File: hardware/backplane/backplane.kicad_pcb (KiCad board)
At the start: 2 copper layers, 199 x 123 mm, 83 parts, among them J1 C96ABC, J10 Conn_Coaxial_Power, J2 C96ABC, J3 C96ABC, J4 C96ABC, J5 C96ABC, J6 C96ABC, J7 C96ABC, J8 C96ABC, J9 C96ABC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

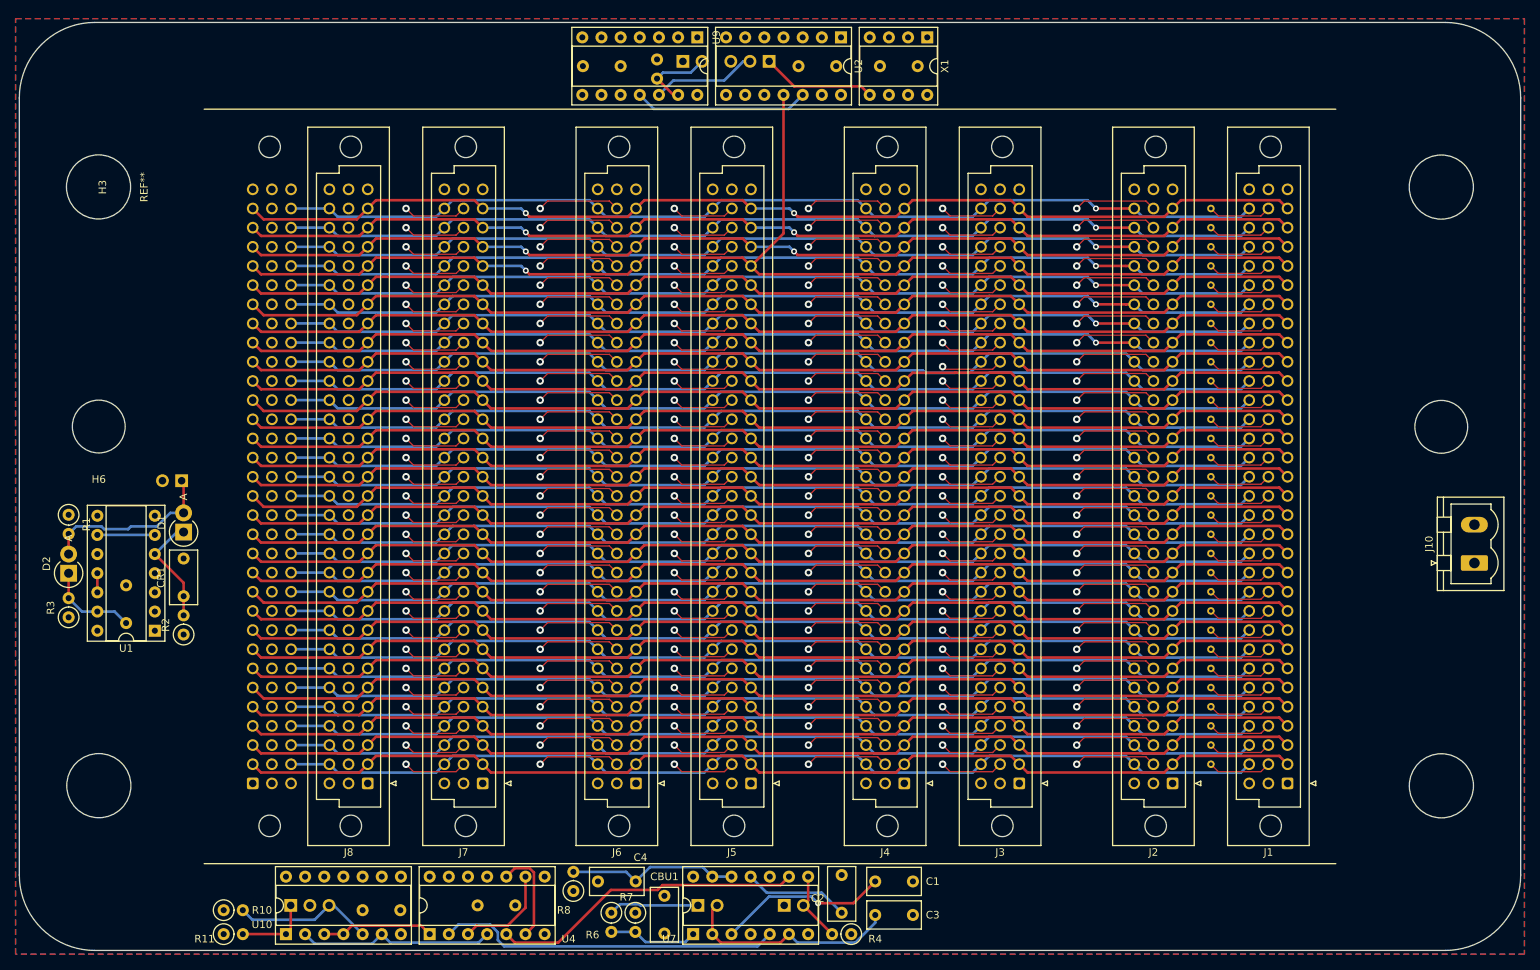
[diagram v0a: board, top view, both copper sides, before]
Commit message: backplane: use mostly SMD parts
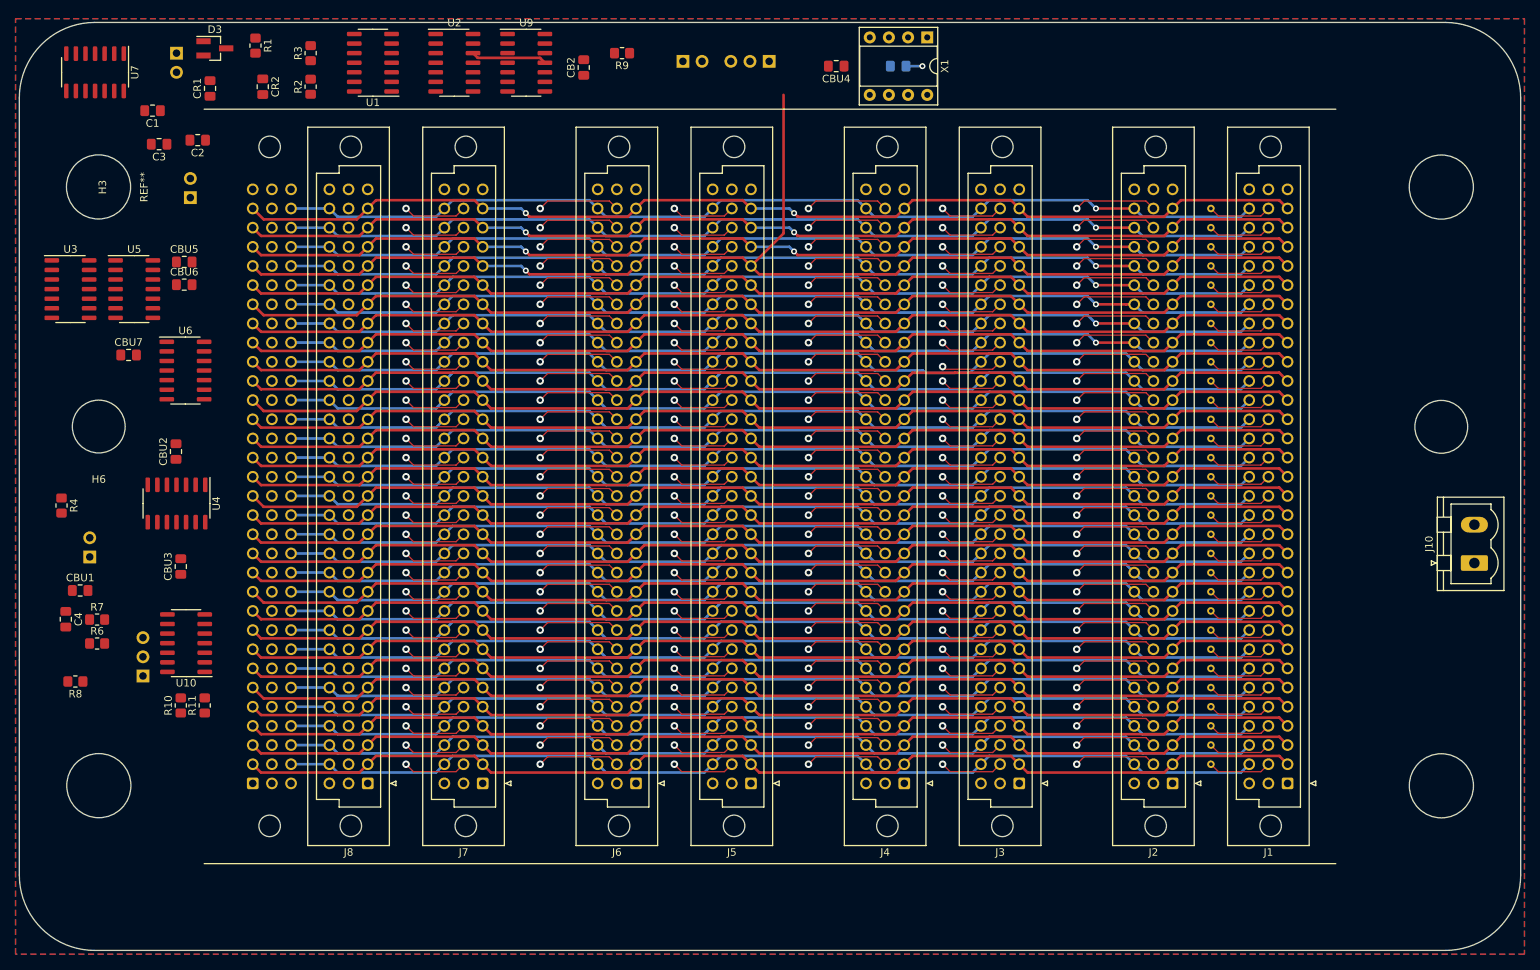
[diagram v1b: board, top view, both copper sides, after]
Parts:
- removed D1, D2: DIODE, Diode_THT:D_DO-15_P2.54mm_Vertical_AnodeUp
- added CBU5: 0.1μF, Capacitor_SMD:C_0805_2012Metric_Pad1.18x1.45mm_HandSolder, F.Cu at (66.4, 60.8)
- added CBU6: 0.1μF, Capacitor_SMD:C_0805_2012Metric_Pad1.18x1.45mm_HandSolder, F.Cu at (66.4, 63.8)
- added CBU7: 0.1μF, Capacitor_SMD:C_0805_2012Metric_Pad1.18x1.45mm_HandSolder, F.Cu at (59.1, 73.1)
- added D3: D_Schottky_x2_KCom_AAK, Package_TO_SOT_SMD:SOT-23_Handsoldering, F.Cu at (70.5, 32.5)
- added U3: 74AHC74, Package_SO:SOIC-14_3.9x8.7mm_P1.27mm, F.Cu at (51.4, 64.4)
- added U5: 74AHC74, Package_SO:SOIC-14_3.9x8.7mm_P1.27mm, F.Cu at (59.8, 64.4)
- added U6: 74AHC02, Package_SO:SOIC-14_3.9x8.7mm_P1.27mm, F.Cu at (66.6, 75.2)
- C1, C2, C3, C4, CBU1, CBX1, CR1: footprint Capacitor_THT:C_Rect_L7.0mm_W3.5mm_P5.00mm -> Capacitor_SMD:C_0805_2012Metric_Pad1.18x1.45mm_HandSolder
- CB2, CBU2, CBU3, CBU4, CR2: footprint Capacitor_THT:C_Rect_L7.0mm_W3.5mm_P5.00mm -> Capacitor_SMD:C_0805_2012Metric_Pad1.18x1.45mm_HandSolder; moved to F.Cu
- R1, R10, R11, R2, R3, R4, R6, R7, R8: footprint Resistor_THT:R_Axial_DIN0207_L6.3mm_D2.5mm_P2.54mm_Vertical -> Resistor_SMD:R_0805_2012Metric_Pad1.20x1.40mm_HandSolder
- R9: footprint Resistor_THT:R_Axial_DIN0207_L6.3mm_D2.5mm_P2.54mm_Vertical -> Resistor_SMD:R_0805_2012Metric_Pad1.20x1.40mm_HandSolder; moved to F.Cu
- U1, U2, U4, U7, U9: footprint Package_DIP:DIP-14_W7.62mm_Socket -> Package_SO:SOIC-14_3.9x8.7mm_P1.27mm
- U10: value U13 -> 74HC00; footprint Package_DIP:DIP-14_W7.62mm_Socket -> Package_SO:SOIC-14_3.9x8.7mm_P1.27mm
- moved C1 140.0 mm to (62.2, 40.7), turned to 180 degrees
- moved C3 139.5 mm to (63.1, 45.2), turned to 180 degrees
- moved U7 139.0 mm to (54.6, 35.6), turned to 270 degrees
- moved C2 133.3 mm to (68.2, 44.6), turned to 180 degrees
- moved SW1 122.5 mm to (67.2, 52.2), turned to 0 degrees
- moved R4 119.1 mm to (50.2, 93.0), turned to 270 degrees
- moved R5 92.9 mm to (53.9, 99.9), turned to 0 degrees
- moved CBU1 87.4 mm to (52.6, 104.3), turned to 0 degrees
- moved C4 83.1 mm to (50.7, 108.1), turned to 270 degrees
- moved R3 81.4 mm to (83.2, 33.1)
- moved R7 81.2 mm to (54.9, 108.2), turned to 0 degrees
- moved U1 80.6 mm to (91.5, 34.4)
- moved R6 76.9 mm to (54.9, 111.3), turned to 0 degrees
- moved R2 74.5 mm to (83.2, 37.5)
- moved CR2 73.4 mm to (76.8, 37.5), turned to 270 degrees
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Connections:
- net Net-(U4-Pad11) renamed PHI_2
- U1 pad 1: GND -> A31
- U1 pad 3: GND -> A28
- U10 pad 10: GND -> Net-(U10-Pad10)
- U10 pad 12: GND -> Net-(U10-Pad12)
- U10 pad 13: GND -> A28
- U10 pad 9: GND -> A31
- U2 pad 4: GND -> Net-(U2-Pad4)
- U2 pad 5: GND -> A27
- U4 pad 12: GND -> Net-(U10-Pad8)
- U4 pad 13: GND -> Net-(U10-Pad11)
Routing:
- net 555_AST: track 45.5 -> 0.00 mm
- net 555_MONO: track 41.6 -> 0.00 mm
- net Net-(C3-Pad1): track 29.2 -> 0.00 mm
- net SEL_MONO: track 26.1 -> 0.00 mm
- net ~RST_HDR~: track 23.7 -> 0.00 mm
- net Net-(C4-Pad1): track 22.8 -> 0.00 mm
- net Net-(C1-Pad1): track 22.7 -> 0.00 mm, vias 1 -> 0
- net Net-(R10-Pad2): track 18.8 -> 0.00 mm
- net XO: track 15.2 -> 0.00 mm
- net SEL_AST: track 14.9 -> 0.00 mm
- net Net-(CR1-Pad1): track 14.7 -> 0.00 mm
- net Net-(C2-Pad1): track 14.0 -> 0.00 mm
- net Net-(SW2-Pad2): track 13.9 -> 0.00 mm
- net Net-(U4-Pad3): track 13.2 -> 0.00 mm
- net Net-(U2-Pad12): track 23.1 -> 10.1 mm
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
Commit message: backplane: place traces
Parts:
- removed the CBU4 at (152.9, 34.8)
- removed R9: 4.7k, Resistor_SMD:R_0805_2012Metric_Pad1.20x1.40mm_HandSolder
- removed U9: 74AHCT125, Package_SO:SOIC-14_3.9x8.7mm_P1.27mm
- added CBU7: 0.1μF, Capacitor_SMD:C_0805_2012Metric_Pad1.18x1.45mm_HandSolder, B.Cu at (65.6, 108.6)
- added CBU8: 0.1μF, Capacitor_SMD:C_0805_2012Metric_Pad1.18x1.45mm_HandSolder, B.Cu at (67.1, 83.0)
- added U8: 74HC00, Package_SO:SOIC-14_3.9x8.7mm_P1.27mm, F.Cu at (66.8, 84.2)
- C1, C2, C3, C4, CBU1, CR1, CR2, X1: moved to B.Cu
- CBU10: renamed from CBU3; moved to B.Cu
- CBU2: renamed from CB2; moved to B.Cu
- CBU3: renamed from CBU5; moved to B.Cu
- CBU4: renamed from CBU2; moved to B.Cu
- CBU5: renamed from CBU6; moved to B.Cu
- CBU6: renamed from CBU7; moved to B.Cu
- CBX1: moved to F.Cu
- R1: value 4.7k -> 1k
- moved X1 134.1 mm to (70.0, 125.8), turned to 90 degrees
- moved CBX1 128.4 mm to (66.6, 121.7)
- moved SW2 121.6 mm to (57.3, 119.5)
- moved JP1 113.6 mm to (53.5, 115.7), turned to 0 degrees
- moved CBU2 78.2 mm to (49.1, 69.1), turned to 270 degrees
- moved U7 74.9 mm to (65.6, 109.8), turned to 0 degrees
- moved C1 71.2 mm to (63.0, 111.9), turned to 270 degrees
- moved C2 68.0 mm to (71.0, 112.6), turned to 270 degrees
- moved U2 64.0 mm to (49.4, 70.5)
- moved C3 62.1 mm to (63.0, 107.2), turned to 90 degrees
- moved SW1 61.7 mm to (57.3, 113.2), turned to 180 degrees
- moved CBU1 45.5 mm to (68.6, 61.7), turned to 270 degrees
- moved U1 36.4 mm to (68.2, 62.4), turned to 0 degrees
- moved R11 31.0 mm to (47.0, 97.8)
- moved SW3 30.2 mm to (48.2, 88.3), turned to 180 degrees
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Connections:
- net PHI_2 renamed Net-(U4-Pad11)
- D3 pad 1: Net-(CR1-Pad1) -> Net-(CR2-Pad1)
- D3 pad 2: Net-(CR2-Pad1) -> Net-(CR1-Pad1)
- JP1 pad 1: GND -> Net-(JP1-Pad1)
- JP1 pad 2: ~CLK_ENABLE~ -> Net-(JP1-Pad2)
- SW2 pad 2: Net-(SW2-Pad2) -> Net-(JP1-Pad1)
- U10 pad 10: Net-(U10-Pad10) -> SEL_AST
- U10 pad 12: Net-(U10-Pad12) -> SEL_MONO
- U10 pad 13: A28 -> 555_MONO
- U10 pad 9: A31 -> 555_AST
- U2 pad 11: A28 -> Net-(U2-Pad11)
- U2 pad 12: Net-(U2-Pad12) -> GND
- U2 pad 13: ~CLK_RST~ -> GND
- U3 pad 9: Net-(U10-Pad10) -> Net-(U3-Pad9)
- U4 pad 1: SEL_AST -> Net-(JP1-Pad2)
- U4 pad 10: Net-(U4-Pad10) -> Net-(U10-Pad11)
- U4 pad 12: Net-(U10-Pad8) -> GND
- U4 pad 13: Net-(U10-Pad11) -> GND
- U4 pad 2: 555_AST -> ~CLK_RST~
- U4 pad 4: SEL_MONO -> Net-(U4-Pad3)
- U4 pad 5: 555_MONO -> Net-(U4-Pad3)
- U4 pad 6: Net-(U4-Pad10) -> A28
- U4 pad 9: Net-(U4-Pad3) -> Net-(U10-Pad8)
- U5 pad 9: Net-(U10-Pad12) -> Net-(U5-Pad9)
- U6 pad 3: Net-(U10-Pad12) -> Net-(U5-Pad9)
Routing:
- net ~CLK_RST~: track 0.00 -> 75.5 mm, vias 0 -> 4
- net C13: track 133.4 -> 208.1 mm
- net A28: track 168.9 -> 221.6 mm, vias 1 -> 4
- net GND: track 0.00 -> 42.8 mm, vias 0 -> 16
- net A31: track 144.7 -> 185.0 mm, vias 2 -> 4
- net A27: track 144.5 -> 179.7 mm
- net 555_CLK: track 0.00 -> 33.8 mm, vias 0 -> 1
- net Net-(JP1-Pad2): track 0.00 -> 30.7 mm, vias 0 -> 1
- net VCC: track 2.18 -> 30.1 mm, vias 1 -> 13
- net Net-(U5-Pad9): track 0.00 -> 25.1 mm, vias 0 -> 2
- net 555_MONO: track 0.00 -> 22.5 mm, vias 0 -> 2
- net Net-(U1-Pad2): track 0.00 -> 22.1 mm, vias 0 -> 2
- net Net-(U2-Pad6): track 0.00 -> 20.8 mm, vias 0 -> 2
- net Net-(U2-Pad4): track 0.00 -> 19.7 mm
- net Net-(C3-Pad1): track 0.00 -> 19.4 mm, vias 0 -> 2
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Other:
- board text removed: "Clock adjust"
- board text removed: "Step"
- board text removed: "astable/mono toggle"

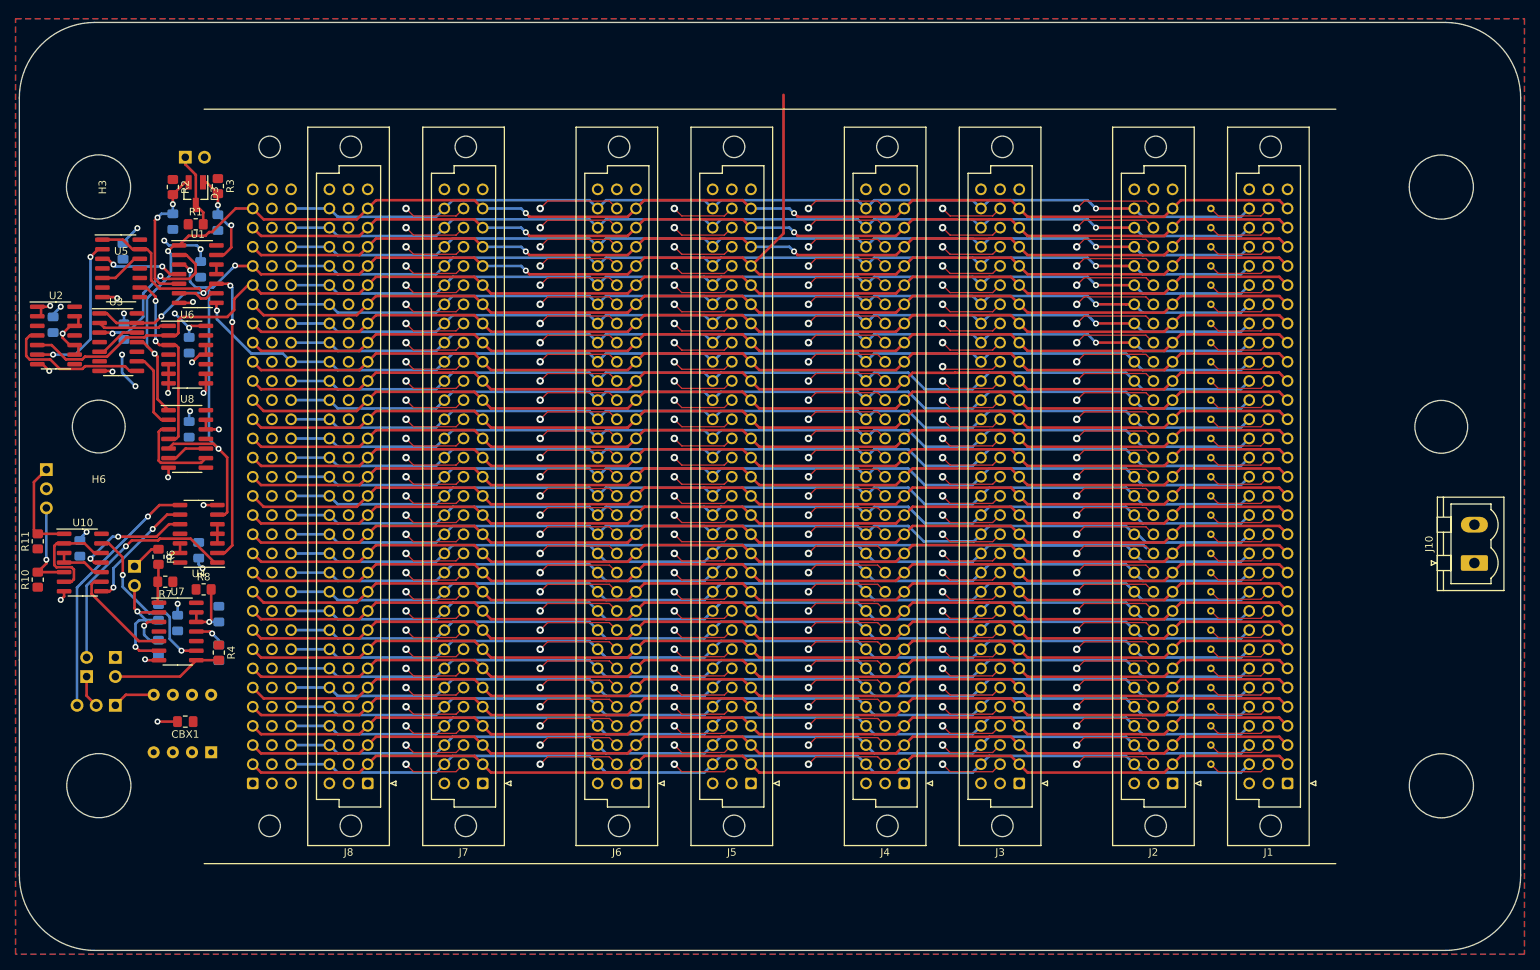
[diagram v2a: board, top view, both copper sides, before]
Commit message: backplane: tweak mounting holes
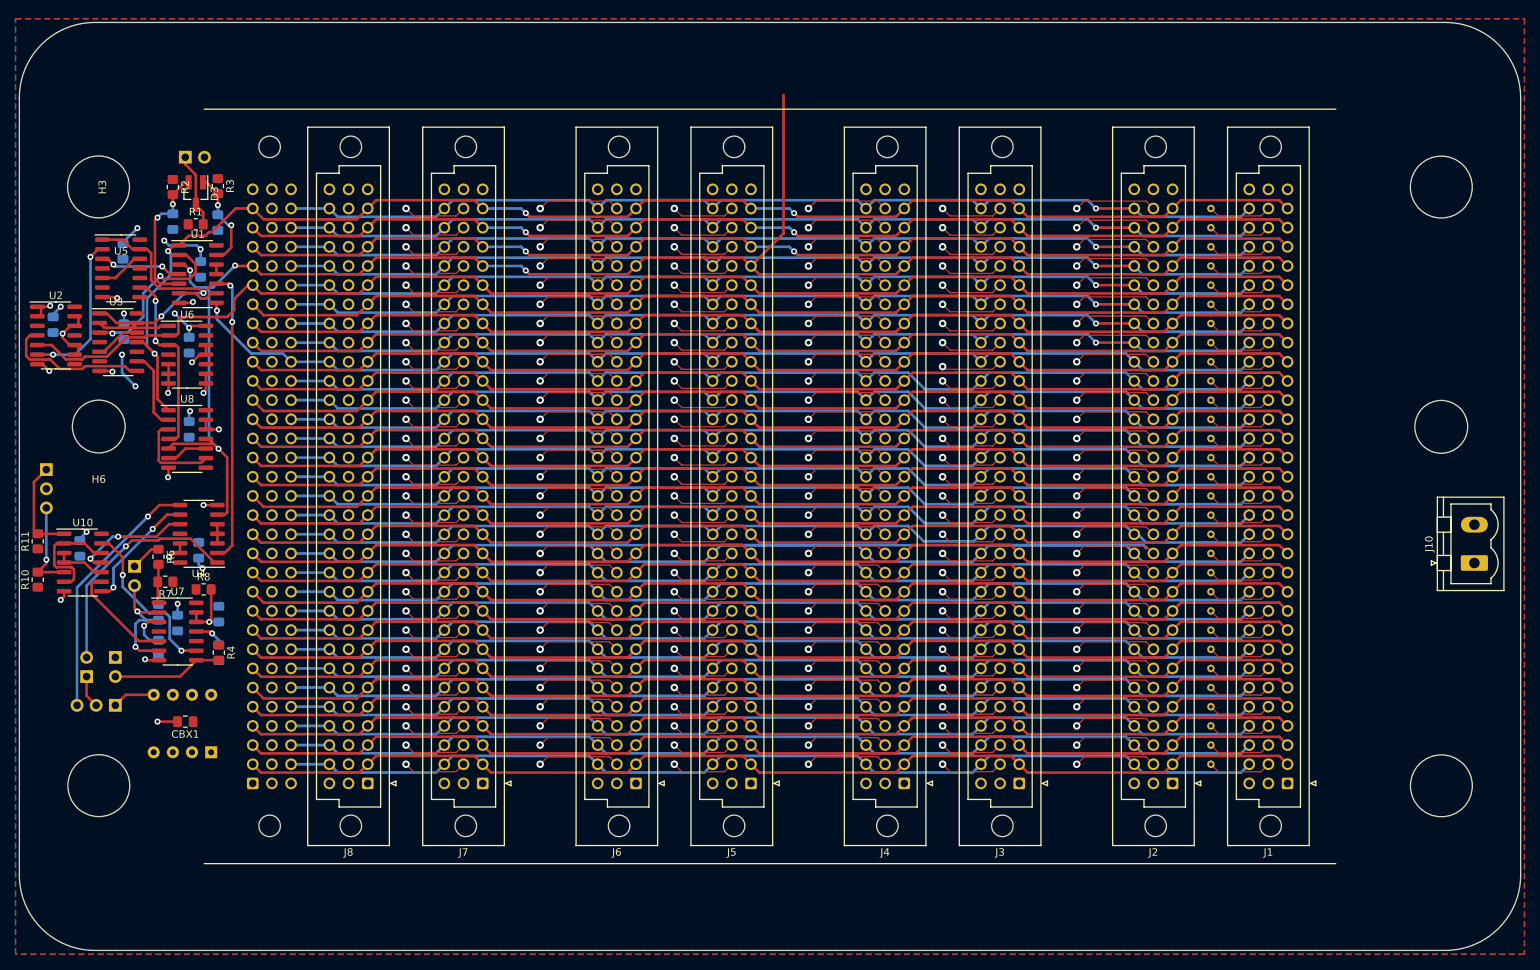
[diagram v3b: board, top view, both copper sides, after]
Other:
- outline, holes or cut-outs redrawn

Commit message: backplane: reduce mounting hardware used
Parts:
- removed H5, H6: MountingHole, rails:7mm
- H1, H2, H4: footprint rails:8mm -> rails:m5-close
- H3: footprint rails:8mm -> rails:m5-close; moved to B.Cu
- moved H4 15.9 mm to (55.1, 146.1), turned to 0 degrees
- moved H2 15.9 mm to (233.0, 35.0), turned to 180 degrees
- moved H3 15.9 mm to (55.2, 35.0), turned to 180 degrees
- moved H1 15.9 mm to (233.0, 146.1), turned to 0 degrees
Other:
- board size 199 x 123 mm -> 200 x 124 mm
